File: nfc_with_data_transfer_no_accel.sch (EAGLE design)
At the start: 8 parts

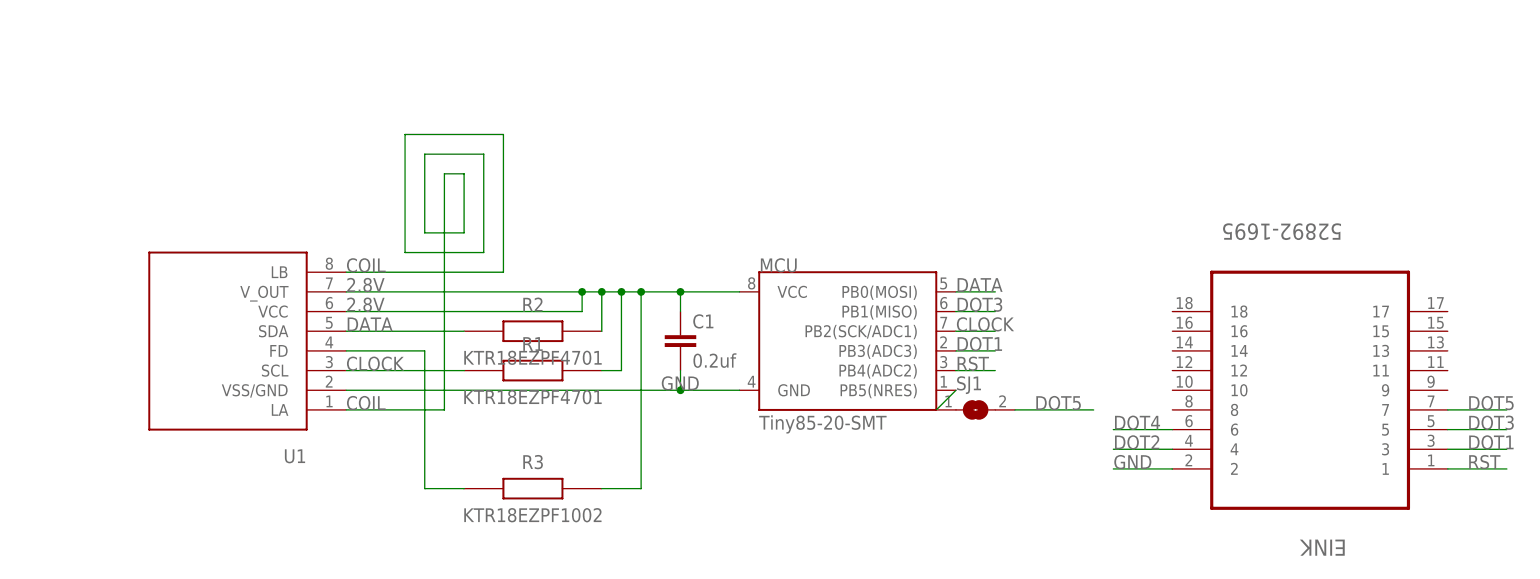
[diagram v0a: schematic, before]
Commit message: Updated board (with traces and embedded coil)
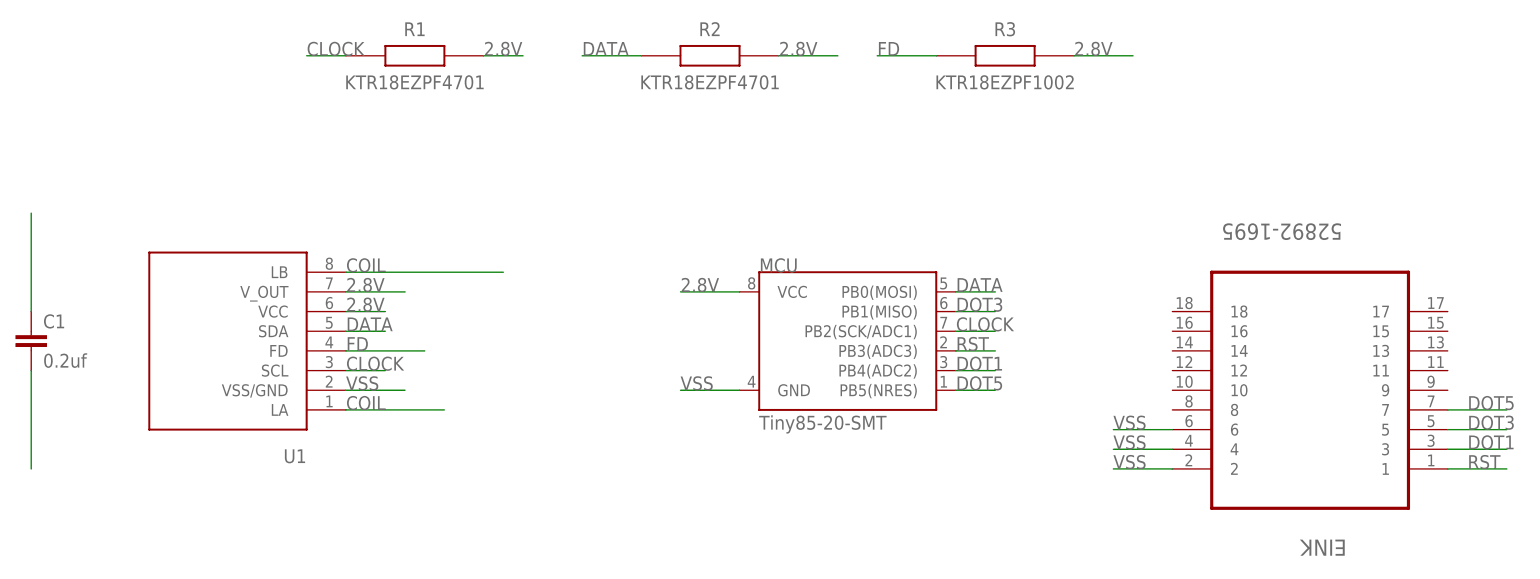
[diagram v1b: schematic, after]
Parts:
- removed SJ1: (no value), microbuilder:SOLDERJUMPER
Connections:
- net N$2 renamed FD
- removed net DOT2: EINK.4
- removed net DOT4: EINK.6
- removed net GND: C1.2, EINK.2, MCU.GND, U1.VSS/GND
- removed net N$1: MCU.PB5(NRES), SJ1.1
- new net VSS: C1.2, EINK.2, EINK.4, EINK.6, MCU.GND, U1.VSS/GND
- net CLOCK: now also R1.1
- net DATA: now also R2.1
- net DOT1: now also MCU.PB4(ADC2); no longer MCU.PB3(ADC3)
- net DOT5: no longer SJ1.2
- net RST: now also MCU.PB3(ADC3); no longer MCU.PB4(ADC2)
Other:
- moved on the sheet: C1, R1, R2, R3
